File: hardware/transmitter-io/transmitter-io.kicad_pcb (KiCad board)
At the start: 2 copper layers, 68.6 x 53.3 mm, 15 parts, among them J1 Output, J2 INPUT, J3 IO EXTENSION, U1 74LS365

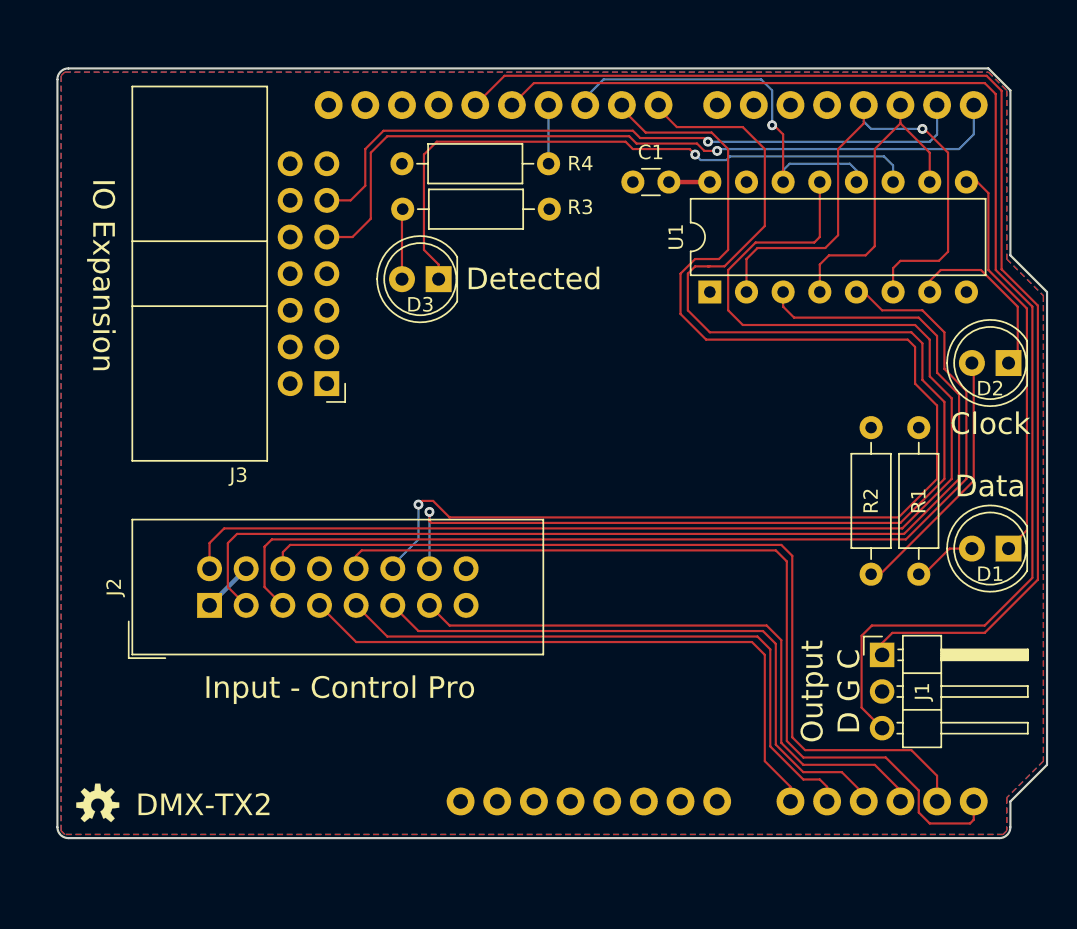
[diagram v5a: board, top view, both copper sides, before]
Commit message: Use 74LS07 Led driver Add R5 for discovery.
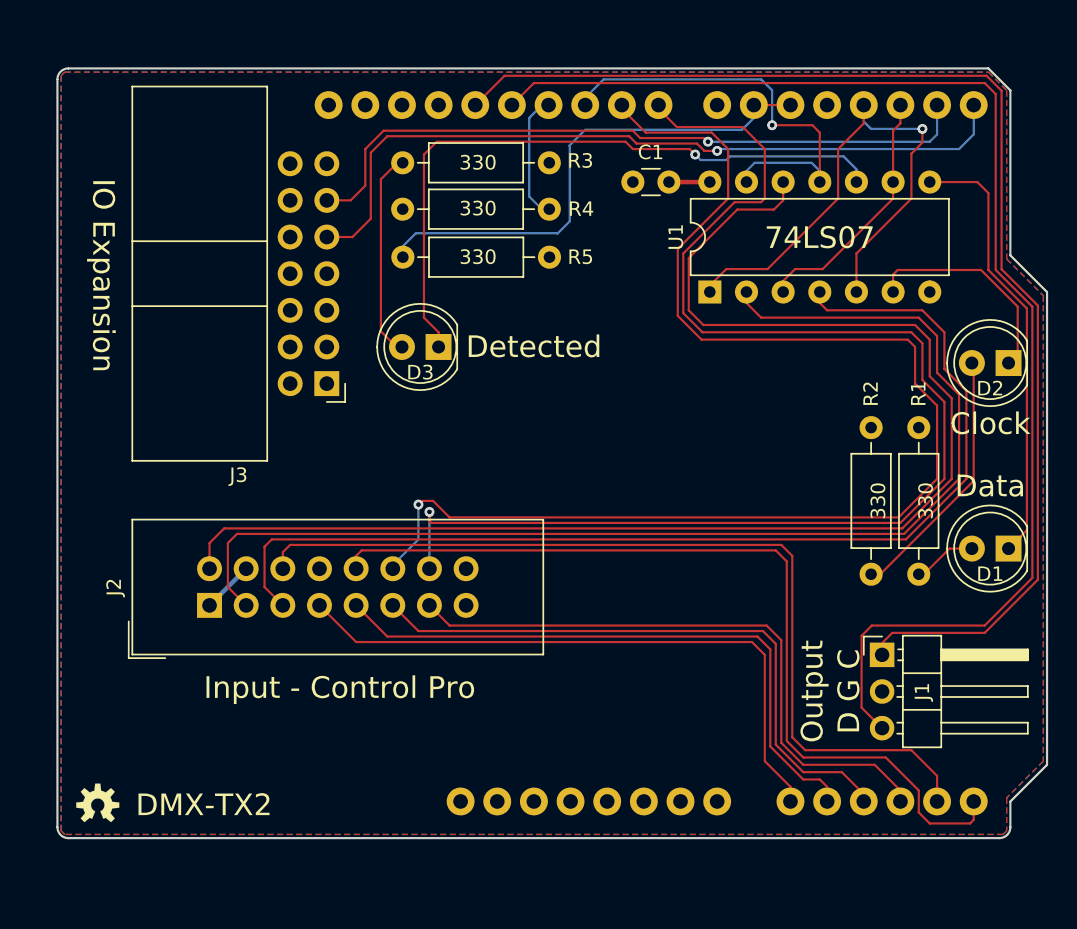
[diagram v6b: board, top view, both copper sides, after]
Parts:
- added R5: 330, Resistor_THT:R_Axial_DIN0207_L6.3mm_D2.5mm_P10.16mm_Horizontal, F.Cu at (150.4, 76.3)
- U1: value 74LS365 -> 74LS07; footprint Package_DIP:DIP-16_W7.62mm -> Package_DIP:DIP-14_W7.62mm
- moved D3 4.70 mm to (142.7, 82.5)
- moved R3 3.21 mm to (150.4, 69.8)
- moved R4 3.15 mm to (150.4, 73.0)
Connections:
- A1 pad 21: Net-(A1-Pad21) -> Net-(A1-Pad20)
- U1 pad 1: GND -> /~CLOCK_OUT
- U1 pad 10: /~DATA_OUT -> Net-(D3-Pad1)
- U1 pad 11: Net-(D3-Pad1) -> /~HWD_DT_OUT
- U1 pad 12: /~HWD_DT_OUT -> /~HWD_DT
- U1 pad 13: /~HWD_DT -> /~HWD_DT_OUT
- U1 pad 14: /~HWD_DT_OUT -> +5V
- U1 pad 2: /~CLOCK_OUT -> /~CLOCK
- U1 pad 3: /~CLOCK -> /~DATA_OUT
- U1 pad 4: /~DATA_OUT -> /~DATA
- U1 pad 5: /~DATA -> /~CLOCK_OUT
- U1 pad 6: /~CLOCK_OUT -> Net-(D2-Pad1)
- U1 pad 7: Net-(D2-Pad1) -> GND
- U1 pad 8: GND -> Net-(D1-Pad1)
- U1 pad 9: Net-(D1-Pad1) -> /~DATA_OUT
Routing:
- net Net-(A1-Pad20): track 0.00 -> 35.3 mm
- net Net-(D3-Pad2): track 4.87 -> 14.4 mm
- net Net-(A1-Pad26): track 4.06 -> 8.90 mm
- net /~DATA_OUT: track 21.7 -> 17.4 mm
- net /~DATA: track 73.2 -> 76.2 mm
- net /~HWD_DT_OUT: track 28.1 -> 30.7 mm
- net Net-(D2-Pad1): track 12.6 -> 15.2 mm
- net Net-(D1-Pad1): track 28.1 -> 30.6 mm
- net /~CLOCK: track 80.4 -> 82.8 mm
- net Net-(D3-Pad1): track 44.0 -> 46.0 mm
- net /~HWD_DT: track 94.3 -> 96.0 mm
- net /~CLOCK_OUT: track 39.7 -> 38.3 mm
- net GND: track 0.00 -> 1.09 mm
- net /~CLK_SLO: track 92.3 -> 91.7 mm
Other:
- board text added: "74LS07"
- board text added: "DMX-TX2, Rev 1.3 Crazy Giraffe Software"
- board text removed: "DMX-TX2, Rev 1.2 Crazy Giraffe Software"
